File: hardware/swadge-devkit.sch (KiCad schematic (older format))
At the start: 60 parts, among them J1 USB_B_Micro, SW1 SW_SPDT, SW2 4-1437565-2, SW3 4-1437565-2, SW4 4-1437565-2, SW5 4-1437565-2, U1 ESP-12F, U2 MCP6001-OT, U3 MSA300, U4 AP1117-33, U5 BUS_PCIexpress, U6 DISP_OLED_UG-2864HSWEG01, U7 2460, U8 2460, U9 MMA8452Q

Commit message: Merged libraries, footprints, and 3d shapes
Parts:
- C1, C10, C11, C12, C13, C14, C15, C16, C17, C18, C19, C2, C20, C21, C22, C3, C4, C5, C6, C7, C8, C9: footprint Capacitor_SMD:C_0603_1608Metric -> Swadge_Parts:C_0603_1608Metric; symbol Device:C -> Swadge_Parts:C
- D1, D2, D3, D4, D5, D6, D7, D8: footprint LED_SMD:LED_WS2812B_PLCC4_5.0x5.0mm_P3.2mm -> Swadge_Parts:LED_WS2812B_PLCC4_5.0x5.0mm_P3.2mm; symbol LED:WS2812B -> Swadge_Parts:WS2812B
- J1: footprint Connector_USB:USB_Micro-B_Molex_47346-0001 -> Swadge_Parts:USB_Micro-B_Molex_47346-0001; symbol Connector:USB_B_Micro -> Swadge_Parts:USB_B_Micro
- MK1: footprint microphone:POM-2738P-R -> Swadge_Parts:POM-2738P-R; symbol Device:Microphone -> Swadge_Parts:Microphone
- R1, R10, R11, R12, R13, R14, R2, R3, R4, R5, R6, R7, R8, R9: footprint Resistor_SMD:R_0603_1608Metric -> Swadge_Parts:R_0603_1608Metric; symbol Device:R_US -> Swadge_Parts:R_US
- SW1: footprint Button_Switch_SMD:SW_SPDT_PCM12 -> Swadge_Parts:SW_SPDT_PCM12; symbol Switch:SW_SPDT -> Swadge_Parts:SW_SPDT
- SW2, SW3, SW4, SW5: footprint 4-1437565-2:SW_4-1437565-2 -> Swadge_Parts:SW_4-1437565-2; symbol 4-1437565-2:4-1437565-2 -> Swadge_Parts:4-1437565-2
- U1: footprint ESP8266:ESP-12E_SMD -> Swadge_Parts:ESP-12E_SMD; symbol ESP8266:ESP-12F -> Swadge_Parts:ESP-12F
- U2: footprint Package_TO_SOT_SMD:SOT-23-5 -> Swadge_Parts:SOT-23-5; symbol Amplifier_Operational:MCP6001-OT -> Swadge_Parts:MCP6001-OT
- U3: footprint MSA300:MSA300 -> Swadge_Parts:MSA300; symbol MSA300:MSA300 -> Swadge_Parts:MSA300
- U4: footprint Package_TO_SOT_SMD:SOT-223-3_TabPin2 -> Swadge_Parts:SOT-223-3_TabPin2; symbol Regulator_Linear:AP1117-33 -> Swadge_Parts:AP1117-33
- U5: footprint Connector_PCBEdge:BUS_PCIexpress -> Swadge_Parts:BUS_PCIexpress; symbol Connector_PCBEdge:BUS_PCIexpress -> Swadge_Parts:BUS_PCIexpress
- U6: footprint disp_oled:microbuilder-UG-2864HSWEG01_1.3_WRAPAROUND -> Swadge_Parts:microbuilder-UG-2864HSWEG01_1.3_WRAPAROUND; symbol disp_oled:DISP_OLED_UG-2864HSWEG01 -> Swadge_Parts:DISP_OLED_UG-2864HSWEG01
- U7, U8: footprint SamacSys_Parts:2460 -> Swadge_Parts:2460; symbol SamacSys_Parts:2460 -> Swadge_Parts:2460
- U9: footprint MMA8452Q:QFN-16_0.5MM -> Swadge_Parts:QFN-16_0.5MM; symbol MMA8452Q:MMA8452Q -> Swadge_Parts:MMA8452Q

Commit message: Made board symmetrical wrt. the PCI connector
Moved batteries to the back, imported Swadge 2019 battery footprint
Reoriented accelerometers so they match orientation
Fattened up power traces
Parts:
- removed U7, U8: 2460, Swadge_Parts:2460, symbol Swadge_Parts:2460
- added BT1, BT2: Battery, Swadge_Parts:BCAAPC, symbol Device:Battery
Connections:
- wire segments 246 -> 240
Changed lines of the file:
@@
 	4950 3450 4300 3450
 Connection ~ 4300 3450
-$Comp
-L Swadge_Parts:2460 U7
-U 1 1 5C3EC94C
-P 9950 1600
-F 0 "U7" V 10304 1728 50  0000 L CNN
-F 1 "2460" V 10395 1728 50  0000 L CNN
-F 2 "Swadge_Parts:2460" H 10600 1700 50  0001 L CNN
-F 3 "https://www.digikey.com/product-detail/en/keystone-electronics/2460/36-2460-ND/280629" H 10600 1600 50  0001 L CNN
-F 4 "Battery Holder; AA; Polypropylene; PC Mount; 1; Spring; PC Lug" H 10600 1500 50  0001 L CNN "Description"
-F 5 "14" H 10600 1400 50  0001 L CNN "Height"
-F 6 "534-2460" H 10600 1300 50  0001 L CNN "Mouser Part Number"
-F 7 "Keystone Electronics" H 10600 1200 50  0001 L CNN "Manufacturer_Name"
-F 8 "2460" H 10600 1100 50  0001 L CNN "Manufacturer_Part_Number"
-	1    9950 1600
-	0    1    1    0
-$EndComp
-Wire Wire Line
-	9950 1600 10400 1600
 Connection ~ 9550 1550
-Wire Wire Line
-	9650 1550 9700 1550
-Wire Wire Line
-	9850 1600 9850 1550
-Connection ~ 9850 1550
-Wire Wire Line
-	9850 1550 10350 1550
-Wire Wire Line
-	9700 2400 9700 1550
-Connection ~ 9700 1550
-Wire Wire Line
-	9700 1550 9850 1550
-$Comp
-L Swadge_Parts:2460 U8
-U 1 1 5C3EC85A
-P 10500 1600
-F 0 "U8" V 10854 1728 50  0000 L CNN
-F 1 "2460" V 10945 1728 50  0000 L CNN
-F 2 "Swadge_Parts:2460" H 11150 1700 50  0001 L CNN
-F 3 "https://www.digikey.com/product-detail/en/keystone-electronics/2460/36-2460-ND/280629" H 11150 1600 50  0001 L CNN
-F 4 "Battery Holder; AA; Polypropylene; PC Mount; 1; Spring; PC Lug" H 11150 1500 50  0001 L CNN "Description"
-F 5 "14" H 11150 1400 50  0001 L CNN "Height"
-F 6 "534-2460" H 11150 1300 50  0001 L CNN "Mouser Part Number"
-F 7 "Keystone Electronics" H 11150 1200 50  0001 L CNN "Manufacturer_Name"
-F 8 "2460" H 11150 1100 50  0001 L CNN "Manufacturer_Part_Number"
-	1    10500 1600
-	0    1    1    0
-$EndComp
-Wire Wire Line
-	10500 1600 10650 1600
 Connection ~ 10050 950
 Wire Wire Line
@@
 Wire Wire Line
 	2700 6900 2700 7000
-Wire Wire Line
-	9700 2400 9850 2400
 Connection ~ 2700 7000
 Wire Wire Line
@@
 Wire Wire Line
 	7800 4950 7800 5000
-Connection ~ 9850 2400
-Wire Wire Line
-	9850 2400 9950 2400
-Connection ~ 9950 2400
-Wire Wire Line
-	9950 2400 10400 2400
-Connection ~ 10400 2400
-Wire Wire Line
-	10400 2400 10500 2400
+$Comp
+L Device:Battery BT2
+U 1 1 5C4A23EF
+P 10450 2000
+F 0 "BT2" V 10205 2000 50  0000 C CNN
+F 1 "Battery" V 10296 2000 50  0000 C CNN
+F 2 "Swadge_Parts:BCAAPC" V 10450 2060 50  0001 C CNN
+F 3 "~" V 10450 2060 50  0001 C CNN
+	1    10450 2000
+	0    1    1    0
+$EndComp
+$Comp
+L Device:Battery BT1
+U 1 1 5C4A255C
+P 10000 2000
+F 0 "BT1" V 9755 2000 50  0000 C CNN
+F 1 "Battery" V 9846 2000 50  0000 C CNN
+F 2 "Swadge_Parts:BCAAPC" V 10000 2060 50  0001 C CNN
+F 3 "~" V 10000 2060 50  0001 C CNN
+	1    10000 2000
+	0    1    1    0
+$EndComp
+Wire Wire Line
+	9650 1550 9800 1550
+Wire Wire Line
+	10650 1600 10650 2000
+Wire Wire Line
+	10250 2000 10200 2000
+Wire Wire Line
+	9800 2000 9800 1550
+Connection ~ 9800 1550
+Wire Wire Line
+	9800 1550 10350 1550
 $EndSCHEMATC

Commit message: Updated library with manufacturing info followiong cnlohr's kicad_for_mfg
Updated all traces (except accelerometer traces) to 0.0077in
Replaced microphone with bigger, cheaper one
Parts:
- BT1, BT2: symbol Device:Battery -> Swadge_Parts:Battery; Cost100 (none) -> 114; Digikey (none) -> BCAAPC-ND; NOBOM (none) -> n; Substitutable (none) -> Y
- C1, C10, C11, C12, C13, C14, C15, C16, C17, C18, C19, C2, C20, C21, C22, C3, C4, C5, C6, C7, C8, C9, R1, R10, R11, R12, R13, R14, R2, R3, R4, R5, R6, R7, R8, R9: Cost100 (none) -> 10; Digikey (none) -> n/a; NOBOM (none) -> n; Substitutable (none) -> Y
- D1, D2, D3, D4, D5, D6, D7, D8: Cost100 (none) -> 45; Digikey (none) -> 1528-1104-ND; NOBOM (none) -> n; Notes (none) -> Digikey item is x10; Substitutable (none) -> Y
- J1: Cost100 (none) -> 112; Digikey (none) -> WM17141CT-ND; NOBOM (none) -> n; Substitutable (none) -> Y
- MK1: footprint Swadge_Parts:POM-2738P-R -> Swadge_Parts:CMA-4544PF-W; Cost100 (none) -> 70; Digikey (none) -> 102-1721-ND; NOBOM (none) -> n; Substitutable (none) -> Y
- SW1: Cost100 (none) -> 96; Digikey (none) -> 401-2016-1-ND; NOBOM (none) -> n; Substitutable (none) -> Y
- SW2, SW3, SW4, SW5: Cost100 (none) -> 34; Description (none) -> Switch Tactile OFF _ON_ SPST Round Button Gull Wing 0.05A 2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; Digikey (none) -> 450-1759-1-ND; Field10 FSM4JSMATR -> (none); Field4 https://www.digikey.com/product-detail/en/te-connectivity-a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 -> (none); Field5 Switch Tactile OFF _ON_ SPST Round Button Gull Wing 0.05A 2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 -> (none); Field6 450-1759-1-ND -> (none); Field7 https://www.te.com/usa-en/product-4-1437565-2.html?te_bu=Co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 -> (none); Field8 TE Connectivity -> (none); Field9 4-1437565-2 -> (none); MPN (none) -> FSM4JSMATR; Manufacturer (none) -> TE Connectivity; NOBOM (none) -> n; Substitutable (none) -> Y
- U1: Cost100 (none) -> 260; Digikey (none) -> Electrodragon SKU NWI1059; NOBOM (none) -> n; Substitutable (none) -> Y
- U2: symbol Swadge_Parts:MCP6001-OT -> Swadge_Parts:MCP6001UT-I_OT; Cost100 (none) -> 25; Digikey (none) -> MCP6001UT-I/OTCT-ND; NOBOM (none) -> n; Substitutable (none) -> Y
- U3: Cost100 (none) -> 34; Digikey (none) -> LCSC Part #C107276; NOBOM (none) -> n; Substitutable (none) -> Y
- U4: symbol Swadge_Parts:AP1117-33 -> Swadge_Parts:AP2114H-3.3TRG1; Cost100 (none) -> 37; Digikey (none) -> AP2114H-3.3TRG1DICT-ND; NOBOM (none) -> n; Substitutable (none) -> Y
- U5: Cost100 (none) -> 0; Digikey (none) -> n/a; NOBOM (none) -> n; Substitutable (none) -> Y
- U6: Cost100 (none) -> 1995; Digikey (none) -> 1528-1512-ND; NOBOM (none) -> n; Substitutable (none) -> Y
- U9: Cost100 (none) -> 264; Digikey (none) -> MMA8452QR1CT-ND; Field4 Unavailable -> (none); Field5 None -> (none); Field6 None -> (none); Field7 NXP Semiconductors -> (none); Field8 MMA8452Q -> (none); Manufacturer (none) -> NXP Semiconductors; NOBOM (none) -> n; Substitutable (none) -> Y
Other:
- note removed: "TODO: Bypass Caps\nTODO: ESP-12F GND on bottom?"

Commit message: Removed NOBOM from parts which didn't need it Added BOM tools
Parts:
- BT1, BT2, C1, C10, C11, C12, C13, C14, C15, C16, C17, C18, C19, C2, C20, C21, C22, C3, C4, C5, C6, C7, C8, C9, D1, D2, D3, D4, D5, D6, D7, D8, J1, MK1, R1, R10, R11, R12, R13, R14, R2, R3, R4, R5, R6, R7, R8, R9, SW1, SW2, SW3, SW4, SW5, U1, U2, U3, U4, U6, U9: NOBOM n -> (none)
- U5: NOBOM n -> y

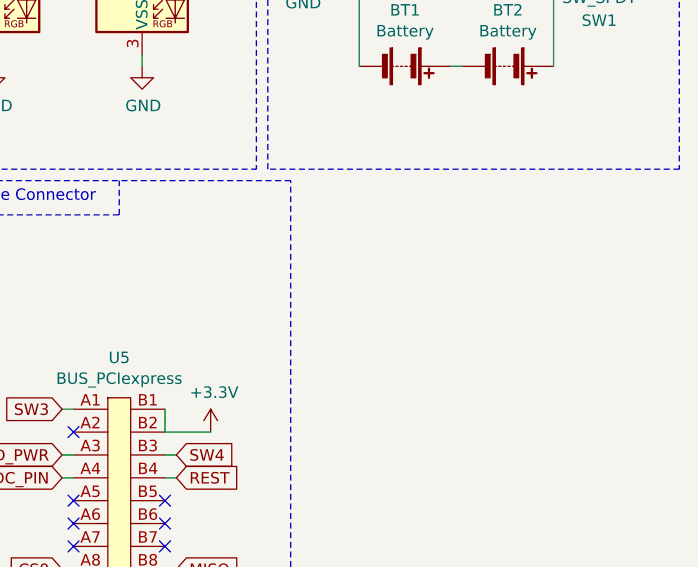
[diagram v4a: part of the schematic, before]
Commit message: Added SAO Moved mic out of the way of buttons Swapped 1.3" display for 0.96" display Linked vishay display instead of adafruit one
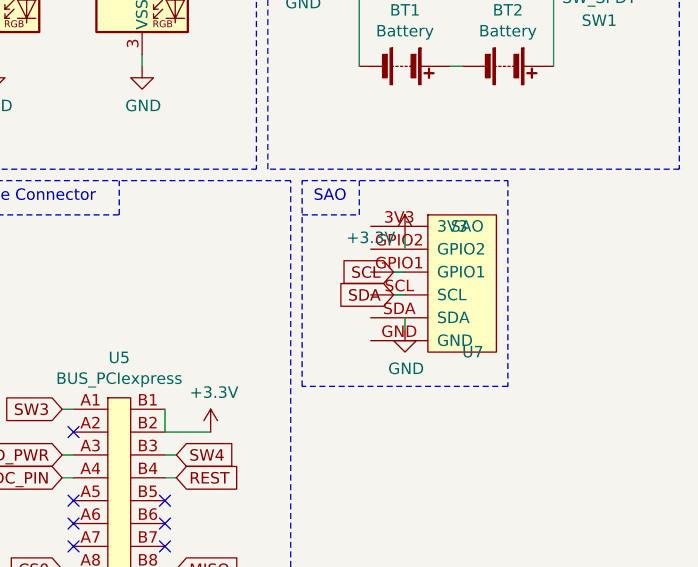
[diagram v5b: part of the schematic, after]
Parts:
- added U7: SAO, Swadge_Parts:SAO, symbol Swadge_Parts:SAO
- U6: footprint Swadge_Parts:microbuilder-UG-2864HSWEG01_1.3_WRAPAROUND -> Swadge_Parts:microbuilder-UG-2864HSWEG01_0.96IN_WRAPAROUND; Adafruit (none) -> https://cdn-shop.adafruit.com/datasheets/UG-2864HSWEG01.pdf; Cost100 1995 -> 988; Digikey 1528-1512-ND -> 541-3485-ND
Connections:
- wire segments 240 -> 244
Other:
- note added: "SAO"
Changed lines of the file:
@@
 F 0 "U6" H 5100 2300 45  0000 L CNN
 F 1 "DISP_OLED_UG-2864HSWEG01" H 5100 2400 45  0000 L CNN
-F 2 "Swadge_Parts:microbuilder-UG-2864HSWEG01_1.3_WRAPAROUND" H 5980 4200 20  0001 C CNN
-F 3 "https://cdn-shop.adafruit.com/datasheets/UG-2864HSWEG01.pdf" H 5950 4050 50  0001 C CNN
-F 4 "1995" H 0   0   50  0001 C CNN "Cost100"
-F 5 "1528-1512-ND" H 0   0   50  0001 C CNN "Digikey"
-F 6 "Y" H 0   0   50  0001 C CNN "Substitutable"
+F 2 "Swadge_Parts:microbuilder-UG-2864HSWEG01_0.96IN_WRAPAROUND" H 5980 4200 20  0001 C CNN
+F 3 "http://www.vishay.com/docs/37903/oled128o064dgpp3n00000.pdf" H 5950 4050 50  0001 C CNN
+F 4 "988" H 0   0   50  0001 C CNN "Cost100"
+F 5 "541-3485-ND" H 0   0   50  0001 C CNN "Digikey"
+F 6 "Y" H 0   0   50  0001 C CNN "Substitutable"
+F 7 "https://cdn-shop.adafruit.com/datasheets/UG-2864HSWEG01.pdf" H 0   0   50  0001 C CNN "Adafruit"
 	1    5950 4050
 	1    0    0    -1
@@
 Wire Wire Line
 	9800 1550 10350 1550
+$Comp
+L Swadge_Parts:SAO U7
+U 1 1 5C708F32
+P 10100 2950
+F 0 "U7" H 10250 2650 50  0000 L CNN
+F 1 "SAO" H 10200 3200 50  0000 L CNN
+F 2 "Swadge_Parts:SAO" H 10050 2600 50  0001 C CNN
+F 3 "https://hackaday.com/2018/06/21/this-is-the-year-conference-badges-get-their-own-badges/shitty-add-on-standard/" H 10150 2700 50  0001 C CNN
+F 4 "0" H 0   0   50  0001 C CNN "Cost100"
+F 5 "n/a" H 0   0   50  0001 C CNN "Digikey"
+F 6 "Y" H 0   0   50  0001 C CNN "NOBOM"
+F 7 "Y" H 0   0   50  0001 C CNN "Substitutable"
+	1    10100 2950
+	1    0    0    -1
+$EndComp
+Text GLabel 9950 2900 0    50   Input ~ 0
+SCL
+Text GLabel 9950 3000 0    50   Input ~ 0
+SDA
+$Comp
+L power:+3.3V #PWR032
+U 1 1 5C7096B1
+P 10000 2750
+F 0 "#PWR032" H 10000 2600 50  0001 C CNN
+F 1 "+3.3V" H 9850 2750 50  0000 C CNN
+F 2 "" H 10000 2750 50  0001 C CNN
+F 3 "" H 10000 2750 50  0001 C CNN
+	1    10000 2750
+	1    0    0    -1
+$EndComp
+$Comp
+L power:GND #PWR033
+U 1 1 5C709736
+P 10000 3150
+F 0 "#PWR033" H 10000 2900 50  0001 C CNN
+F 1 "GND" H 10005 2977 50  0000 C CNN
+F 2 "" H 10000 3150 50  0001 C CNN
+F 3 "" H 10000 3150 50  0001 C CNN
+	1    10000 3150
+	1    0    0    -1
+$EndComp
+Wire Wire Line
+	10000 2750 10000 2800
+Wire Wire Line
+	9950 2900 10000 2900
+Wire Wire Line
+	9950 3000 10000 3000
+Wire Wire Line
+	10000 3100 10000 3150
+Wire Notes Line
+	9550 2500 10450 2500
+Wire Notes Line
+	10450 2500 10450 3400
+Wire Notes Line
+	10450 3400 9550 3400
+Wire Notes Line
+	9550 3400 9550 2500
+Text Notes 9600 2600 0    50   ~ 0
+SAO
+Wire Notes Line
+	9550 2650 9800 2650
+Wire Notes Line
+	9800 2650 9800 2500
 $EndSCHEMATC

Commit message: Added digikey part numbers for passives Updated PCB color swatch, logo Added name & version to PCB
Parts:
- C1: Digikey n/a -> 490-7611-1-ND
- C10, C11, C4, C5, C6, C7, C8, C9: Digikey n/a -> 1276-1036-1-ND
- C12, C13, C14, C21, C22: Digikey n/a -> 1276-1000-1-ND
- C15, C16, C17, C19: value 2.2u -> 1u; Digikey n/a -> 1276-1036-1-ND
- C18: Digikey n/a -> 1276-1885-1-ND
- C2, C3: Digikey n/a -> 587-1249-1-ND
- C20: Digikey n/a -> 490-10469-1-ND
- R1: Digikey n/a -> RMCF0603FT1K00DKR-ND
- R10, R11, R3, R5, R6, R9: Digikey n/a -> RNCP0603FTD10K0CT-ND
- R12, R13, R2, R4: Digikey n/a -> 311-4.70KHRCT-ND
- R14: Digikey n/a -> 311-390KHRCT-ND
- R7: Digikey n/a -> 311-220HRCT-ND
- R8: Digikey n/a -> 311-71.5HRCT-ND
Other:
- moved on the sheet: R14

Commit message: Updated digikey part numbers Added graphics to swadge programmer PCB
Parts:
- C18: Digikey 1276-1885-1-ND -> 1276-1085-1-ND
- U6: Digikey 541-3485-ND -> 541-3486-ND
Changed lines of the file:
@@
 F 3 "http://www.vishay.com/docs/37903/oled128o064dgpp3n00000.pdf" H 5950 4050 50  0001 C CNN
 F 4 "988" H 0   0   50  0001 C CNN "Cost100"
-F 5 "541-3485-ND" H 0   0   50  0001 C CNN "Digikey"
+F 5 "541-3486-ND" H 0   0   50  0001 C CNN "Digikey"
 F 6 "Y" H 0   0   50  0001 C CNN "Substitutable"
 F 7 "https://cdn-shop.adafruit.com/datasheets/UG-2864HSWEG01.pdf" H 0   0   50  0001 C CNN "Adafruit"
@@
 F 3 "" H 4250 5400 50  0001 C CNN
 F 4 "10" H 0   0   50  0001 C CNN "Cost100"
-F 5 "1276-1885-1-ND" H 0   0   50  0001 C CNN "Digikey"
+F 5 "1276-1085-1-ND" H 0   0   50  0001 C CNN "Digikey"
 F 6 "Y" H 0   0   50  0001 C CNN "Substitutable"
 	1    4250 5400

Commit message: Updated digikey part numbers
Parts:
- R1: Digikey RMCF0603FT1K00DKR-ND -> 311-1.00KHRCT-ND
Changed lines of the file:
@@
 F 3 "" H 2950 700 50  0001 C CNN
 F 4 "10" H 0   0   50  0001 C CNN "Cost100"
-F 5 "RMCF0603FT1K00DKR-ND" H 0   0   50  0001 C CNN "Digikey"
+F 5 "311-1.00KHRCT-ND" H 0   0   50  0001 C CNN "Digikey"
 F 6 "Y" H 0   0   50  0001 C CNN "Substitutable"
 	1    2950 700
